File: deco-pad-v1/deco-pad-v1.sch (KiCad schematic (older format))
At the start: 23 parts

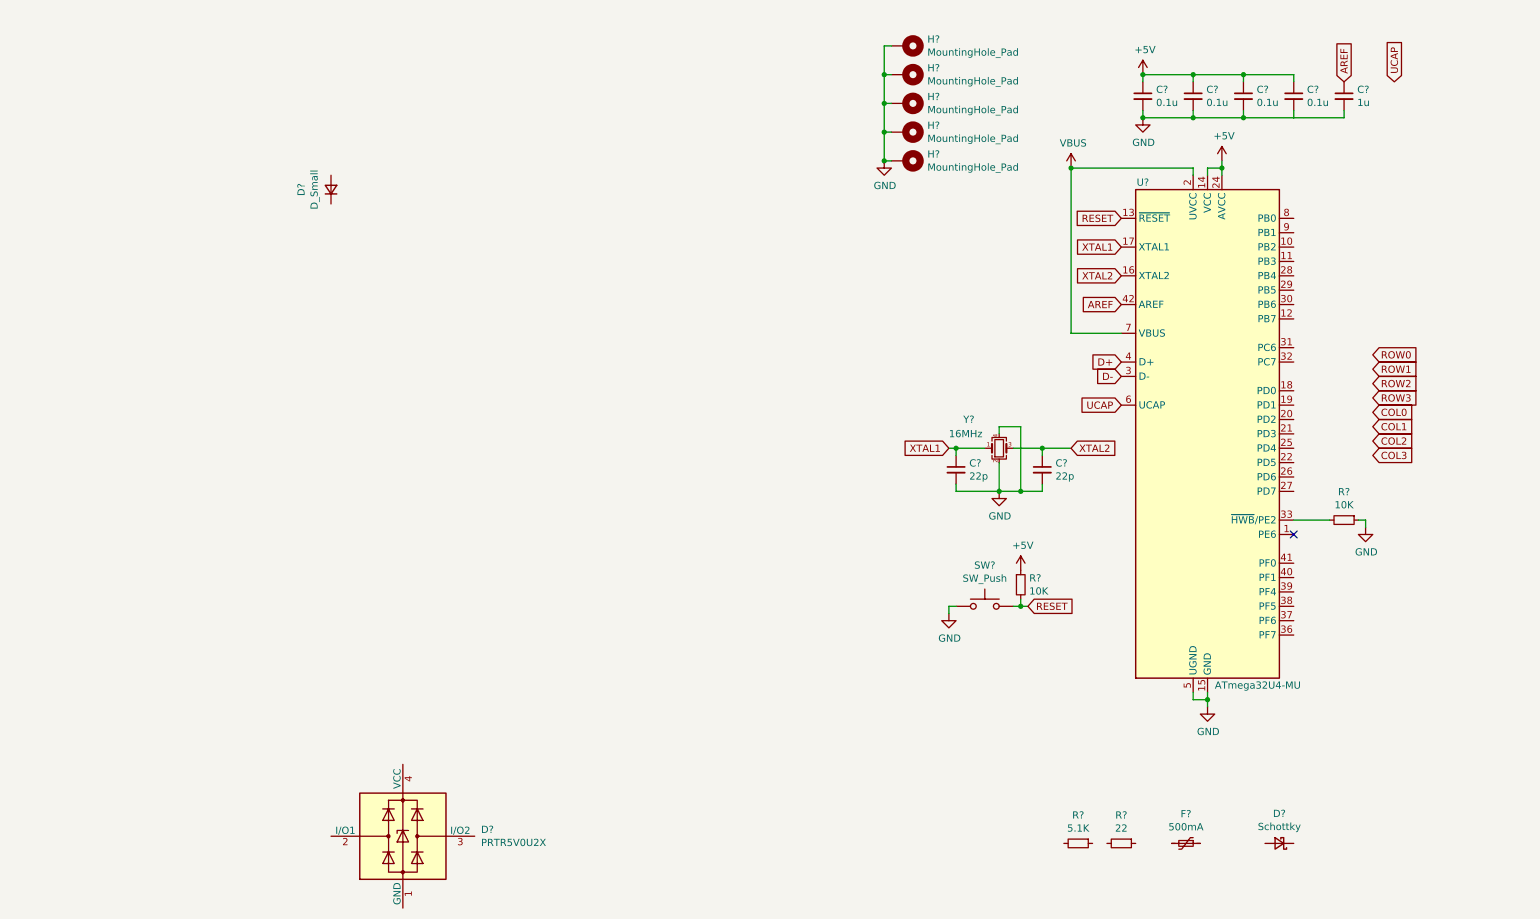
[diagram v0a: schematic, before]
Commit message: [NZ] Almost completed on schematic and choosing footprints.
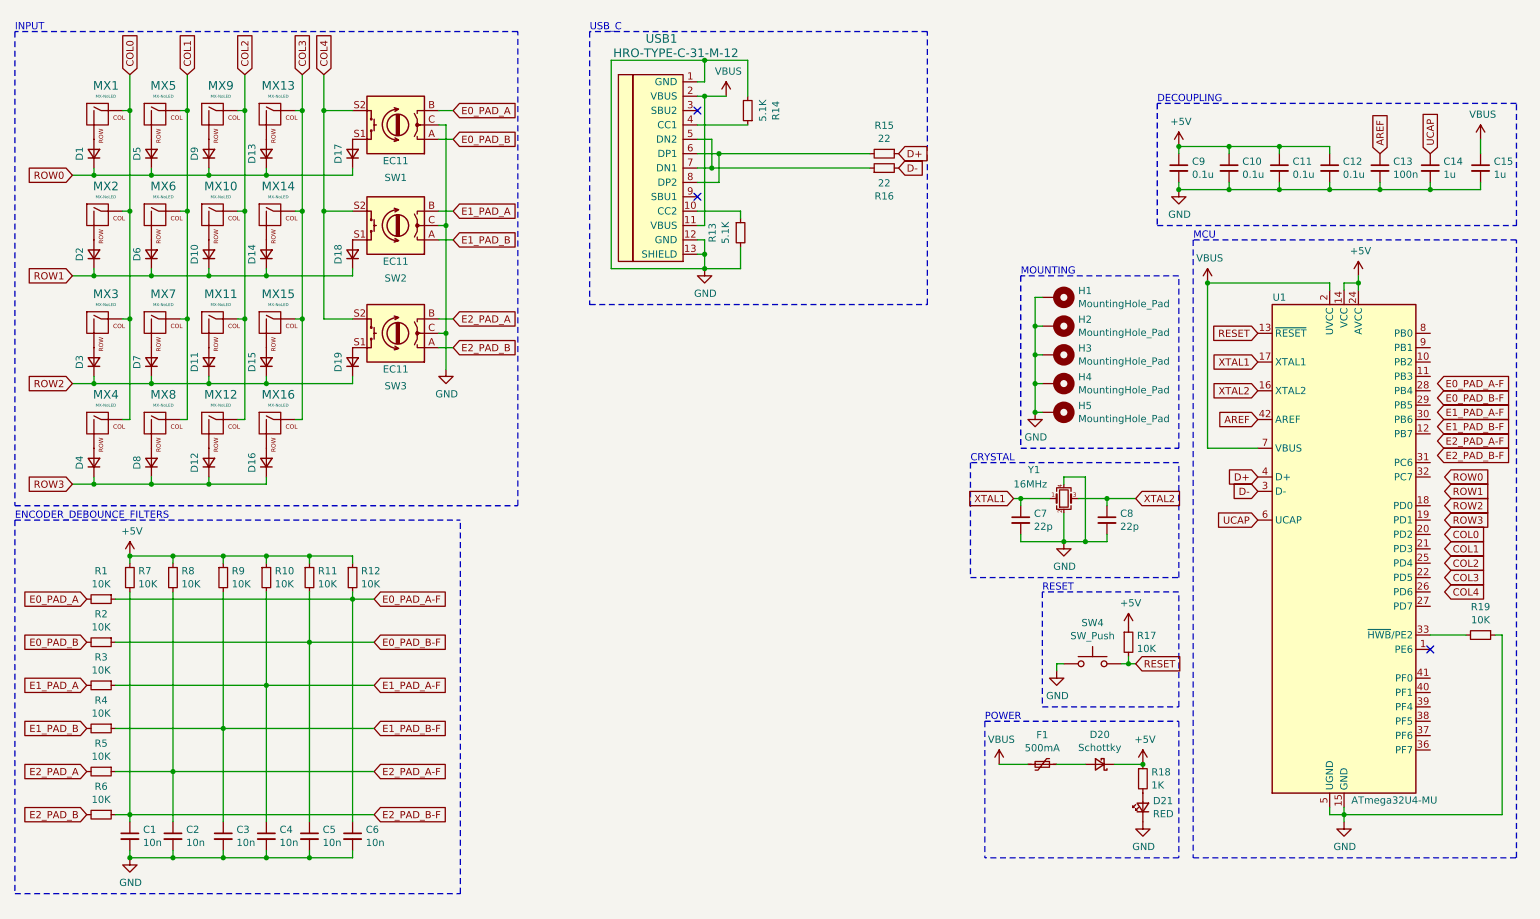
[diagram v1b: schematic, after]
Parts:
- removed D?: PRTR5V0U2X, Package_TO_SOT_SMD:SOT-143, symbol Power_Protection:PRTR5V0U2X
- removed D?: D_Small, symbol Device:D_Small
- added C1, C2, C3, C4, C5, C6: 10n, Capacitor_SMD:C_0603_1608Metric, symbol Device:C_Small
- added C14: 1u, Capacitor_SMD:C_0603_1608Metric, symbol Device:C_Small
- added C15: 1u, Capacitor_SMD:C_0805_2012Metric, symbol Device:C_Small
- added D1, D10, D11, D12, D13, D14, D15, D16, D17, D18, D19, D2, D3, D4, D5, D6, D7, D8, D9: D_Small, symbol Device:D_Small
- added D21: RED, symbol Device:LED_Small
- added MX1, MX10, MX11, MX12, MX13, MX14, MX15, MX16, MX2, MX3, MX4, MX5, MX6, MX7, MX8, MX9: MX-NoLED, symbol MX_Alps_Hybrid:MX-NoLED
- added R1, R10, R11, R12, R2, R3, R4, R5, R6, R7, R8, R9: 10K, symbol Device:R_Small
- added R14: 5.1K, symbol Device:R_Small
- added R15: 22, symbol Device:R_Small
- added R18: 1K, symbol Device:R_Small
- added SW1, SW2, SW3: EC11, symbol Device:Rotary_Encoder_Switch
- added USB1: HRO-TYPE-C-31-M-12, type-c:HRO-TYPE-C-31-M-12-HandSoldering, symbol Type-C:HRO-TYPE-C-31-M-12
- C10, C11, C12, C7, C8, C9: renamed from C?; footprint (none) -> Capacitor_SMD:C_0603_1608Metric
- C13: renamed from C?; value 1u -> 100n; footprint (none) -> Capacitor_SMD:C_0603_1608Metric
- H1, H2, H3, H4, H5: renamed from H?; footprint (none) -> MountingHole:MountingHole_2.2mm_M2_Pad_Via
- gave numbers to parts that had none: 9
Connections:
- net +5V: now also D20.1 (K), R10.1, R11.1, R12.1, R18.1, R7.1, R8.1, R9.1
- net COL0: now also MX1.1 (COL), MX2.1 (COL), MX3.1 (COL), MX4.1 (COL)
- net COL1: now also MX5.1 (COL), MX6.1 (COL), MX7.1 (COL), MX8.1 (COL)
- net COL2: now also MX10.1 (COL), MX11.1 (COL), MX12.1 (COL), MX9.1 (COL)
- net COL3: now also MX13.1 (COL), MX14.1 (COL), MX15.1 (COL), MX16.1 (COL)
- net D+: now also R15.1
- net D-: now also R16.2
- net GND: now also R13.2, C1.2, C14.2, C15.2, C2.2, C3.2, C4.2, C5.2, C6.2, D21.1 (K), R14.2, SW1.C, SW2.C, SW3.C, USB1.1 (GND), USB1.12 (GND), USB1.13 (SHIELD)
- net ROW0: now also D1.1 (K), D13.1 (K), D17.1 (K), D5.1 (K), D9.1 (K)
- net ROW1: now also D10.1 (K), D14.1 (K), D18.1 (K), D2.1 (K), D6.1 (K)
- net ROW2: now also D11.1 (K), D15.1 (K), D19.1 (K), D3.1 (K), D7.1 (K)
- net ROW3: now also D12.1 (K), D16.1 (K), D4.1 (K), D8.1 (K)
- net UCAP: now also C14.1
- net VBUS: now also F1.2, C15.1, USB1.11 (VBUS), USB1.2 (VBUS)
- net at F1.1: now also D20.2 (A)
- net at R13.1: now also USB1.10 (CC2)
- net at R16.1: now also USB1.5 (DN2), USB1.7 (DN1)
- new net: R14.1, USB1.4 (CC1)
- new net: R15.2, USB1.6 (DP1), USB1.8 (DP2)
- new net: D1.2 (A), MX1.2 (ROW)
- new net: D5.2 (A), MX5.2 (ROW)
- new net: D9.2 (A), MX9.2 (ROW)
- new net: D13.2 (A), MX13.2 (ROW)
- new net: D19.2 (A), SW3.S1
- new net: D18.2 (A), SW2.S1
- new net: D17.2 (A), SW1.S1
- new net: D2.2 (A), MX2.2 (ROW)
- new net: D6.2 (A), MX6.2 (ROW)
- new net: D10.2 (A), MX10.2 (ROW)
- new net: D14.2 (A), MX14.2 (ROW)
- new net: D3.2 (A), MX3.2 (ROW)
- new net: D7.2 (A), MX7.2 (ROW)
- new net: D11.2 (A), MX11.2 (ROW)
- new net: D15.2 (A), MX15.2 (ROW)
- new net: D4.2 (A), MX4.2 (ROW)
- new net: D8.2 (A), MX8.2 (ROW)
- new net: D12.2 (A), MX12.2 (ROW)
- new net: D16.2 (A), MX16.2 (ROW)
- new net: D21.2 (A), R18.2
- new net COL4: SW1.S2, SW2.S2, SW3.S2
- new net E0_PAD_A: R1.2, SW1.B
- new net E0_PAD_A-F: C6.1, R1.1, R12.2
- new net E0_PAD_B: R2.2, SW1.A
- new net E0_PAD_B-F: C5.1, R11.2, R2.1
- new net E1_PAD_A: R3.2, SW2.B
- new net E1_PAD_A-F: C4.1, R10.2, R3.1
- new net E1_PAD_B: R4.2, SW2.A
- new net E1_PAD_B-F: C3.1, R4.1, R9.2
- new net E2_PAD_A: R5.2, SW3.B
- new net E2_PAD_A-F: C2.1, R5.1, R8.2
- new net E2_PAD_B: R6.2, SW3.A
- new net E2_PAD_B-F: C1.1, R6.1, R7.2
- no-connect marks 1 -> 3
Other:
- note added: "CRYSTAL"
- note added: "DECOUPLING"
- note added: "ENCODER_DEBOUNCE_FILTERS"
- note added: "INPUT"
- note added: "MCU"
- note added: "MOUNTING"
- note added: "POWER"
- note added: "RESET"
- note added: "USB_C"
- moved on the sheet: C10, C11, C12, C13, C7, C8, C9, D20, F1, H1, H2, H3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

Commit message: [NZ] Schematic and Footprints done.
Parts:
- added J1: AVR-ISP-6, Connector_PinSocket_2.54mm:PinSocket_2x03_P2.54mm_Vertical, symbol Connector:AVR-ISP-6
- added U2: PRTR5VOU2X, Nexperia:SOT143B, symbol prtr5vou2x:PRTR5VOU2X
- C1, C10, C11, C12, C13, C14, C2, C3, C4, C5, C6, C7, C8, C9: footprint Capacitor_SMD:C_0603_1608Metric -> Capacitor_SMD:C_0805_2012Metric
- D1, D10, D11, D12, D13, D14, D15, D16, D17, D18, D19, D2, D20, D3, D4, D5, D6, D7, D8, D9: footprint (none) -> Diode_SMD:D_SOD-123
- D21: footprint (none) -> LED_SMD:LED_0805_2012Metric
- F1: footprint (none) -> Fuse:Fuse_1206_3216Metric
- MX1, MX10, MX11, MX12, MX13, MX14, MX15, MX16, MX2, MX3, MX4, MX5, MX6, MX7, MX8, MX9: footprint (none) -> mx-alps-hybrid:MX-1U-NoLED
- R1, R10, R11, R12, R13, R14, R15, R16, R17, R18, R19, R2, R3, R4, R5, R6, R7, R8, R9: footprint (none) -> Resistor_SMD:R_0805_2012Metric
- SW1, SW2, SW3: footprint (none) -> Rotary_Encoder:RotaryEncoder_Alps_EC11E-Switch_Vertical_H20mm
- SW4: footprint (none) -> Button_Switch_SMD:SW_SPST_B3S-1000
- Y1: footprint (none) -> Crystal:Crystal_SMD_3225-4Pin_3.2x2.5mm
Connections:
- net +5V: now also J1.2 (VCC)
- net COL0: now also U1.25 (PD4)
- net COL1: now also U1.26 (PD6)
- net COL2: now also U1.27 (PD7)
- net COL3: now also U1.28 (PB4)
- net COL4: now also U1.29 (PB5)
- net D+: now also R16.2; no longer R15.1
- net D-: now also R15.1; no longer R16.2
- net E0_PAD_A-F: now also U1.36 (PF7)
- net E0_PAD_B-F: now also U1.37 (PF6)
- net E1_PAD_A-F: now also U1.38 (PF5)
- net E1_PAD_B-F: now also U1.39 (PF4)
- net E2_PAD_A-F: now also U1.40 (PF1)
- net E2_PAD_B-F: now also U1.41 (PF0)
- net GND: now also J1.6 (GND), U2.1 (GND)
- net RESET: now also J1.5 (~RST)
- net ROW0: now also U1.18 (PD0)
- net ROW1: now also U1.19 (PD1)
- net ROW2: now also U1.20 (PD2)
- net ROW3: now also U1.21 (PD3)
- net VBUS: now also U2.4 (VCC)
- net MISO: now reaches U1.10 (PB2)
- net MISO: now also J1.1 (MISO)
- net MOSI: now reaches U1.11 (PB3)
- net MOSI: now also J1.4 (MOSI)
- net SCK: now reaches U1.9 (PB1)
- net SCK: now also J1.3 (SCK)
- net at USB1.5 (DN2), USB1.7 (DN1): now also R15.2, U2.3 (IO2); no longer R16.1
- net at USB1.6 (DP1), USB1.8 (DP2): now also R16.1, U2.2 (IO1); no longer R15.2
- no-connect marks 3 -> 9
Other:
- note added: "ISP"
- moved on the sheet: C1, C10, C11, C12, C13, C14, C15, C2, C3, C4, C5, C6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
